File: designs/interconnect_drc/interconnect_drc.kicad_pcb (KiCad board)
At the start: 2 copper layers, 90.7 x 60.5 mm, 1 part

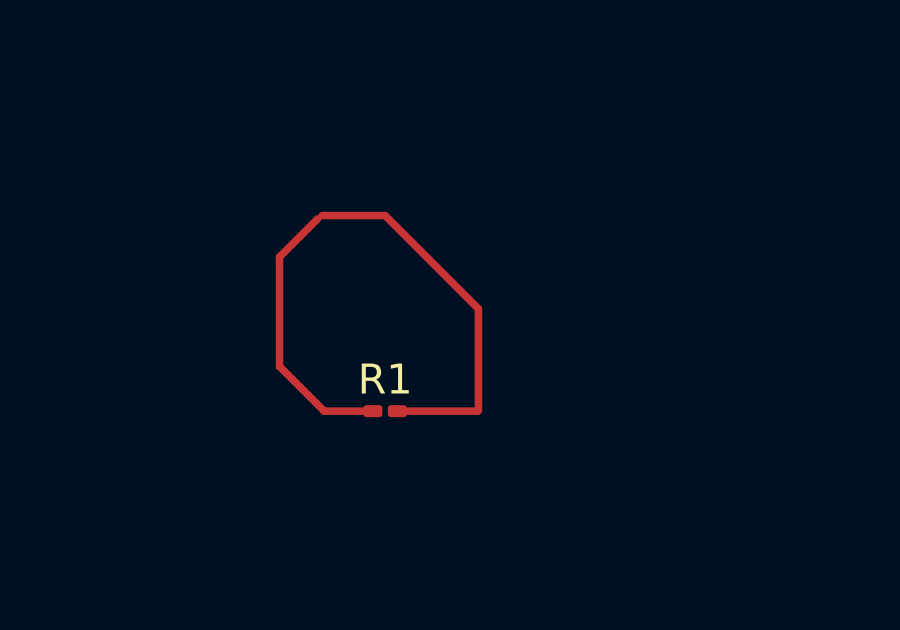
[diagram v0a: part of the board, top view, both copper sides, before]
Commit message: Convert to teardrop testcase
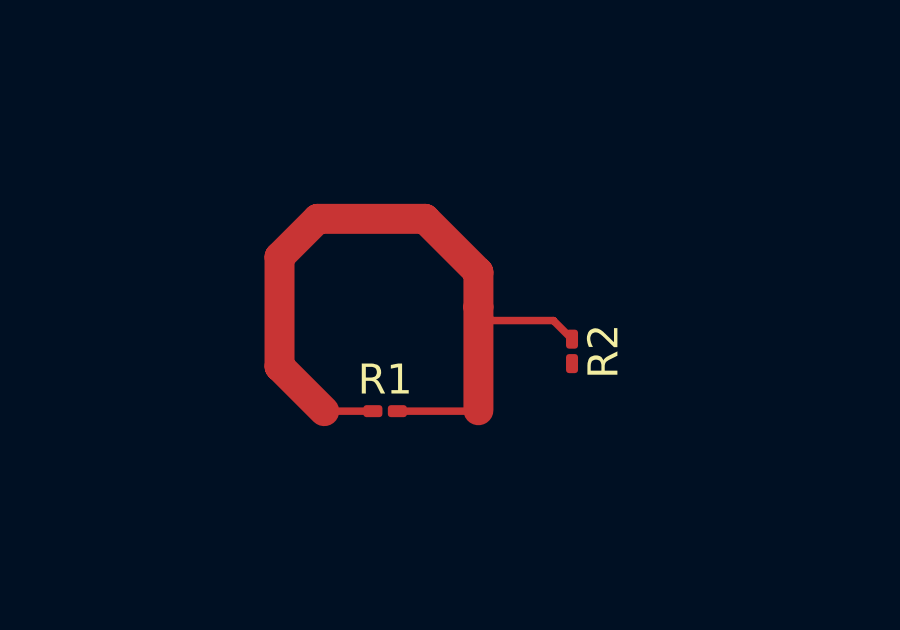
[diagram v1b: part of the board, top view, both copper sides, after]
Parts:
- added R2: R_Small, Resistor_SMD:R_0201_0603Metric_Pad0.64x0.40mm_HandSolder, F.Cu at (132.4, 82.0)
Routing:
- net Net-(R1-Pad1): track 21.8 -> 26.2 mm

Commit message: Rename to tc6
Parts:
- removed R1, R2: R_Small, Resistor_SMD:R_0201_0603Metric_Pad0.64x0.40mm_HandSolder
- added J1: Screw_Terminal_01x08, Project:TerminalBlock_Phoenix_MKDS_1727078_1x08_P3.81mm_Horizontal, F.Cu at (155.1, 146.1)
- added R3: R_Small, Resistor_SMD:R_0805_2012Metric, F.Cu at (129.5, 133.8)
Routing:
- net GND: track 0.00 -> 86.3 mm, vias 0 -> 2
- net +3V3: track 0.00 -> 58.9 mm, vias 0 -> 2
- net Net-(J1-Pin_3): track 0.00 -> 53.2 mm, vias 0 -> 2
- net Net-(J1-Pin_2): track 0.00 -> 32.3 mm, vias 0 -> 1
- net (no net): track 0.00 -> 27.7 mm, vias 0 -> 2
- net Net-(R1-Pad1): track 26.2 -> 0.00 mm
- net unconnected-(J1-Pin_6-Pad6): track 0.00 -> 13.2 mm, vias 0 -> 1
- added copper zone on F.Cu, net +3V3
